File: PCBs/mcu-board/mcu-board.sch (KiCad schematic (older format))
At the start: 7 parts, among them J1 ENCODER-PANEL-1, J2 ENCODER-PANEL-2, J3 5V, J4 3.3V, J5 MDAC-INPUT-SELECTOR, U1 m0-express

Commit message: Updating mcu-board PCB
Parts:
- added C1, C2: C, Capacitor_SMD:C_1206_3216Metric_Pad1.42x1.75mm_HandSolder, symbol Device:C
- added H1, H2, H3, H4: MountingHole_Pad, MountingHole:MountingHole_3.2mm_M3_Pad, symbol Mechanical:MountingHole_Pad
- added IR1: Conn_01x03, Connector_Molex:Molex_KK-254_AE-6410-03A_1x03_P2.54mm_Vertical, symbol Connector_Generic:Conn_01x03
- added LED_3V1, LED_5V1: LED, LED_SMD:LED_1206_3216Metric_Pad1.42x1.75mm_HandSolder, symbol Device:LED
- added RLED1, RLED2: R, Resistor_SMD:R_1206_3216Metric_Pad1.42x1.75mm_HandSolder, symbol Device:R
- added U2, U3: SN74AHCT125DR, Package_SO:SOIC-14_3.9x8.7mm_P1.27mm, symbol SN74AHCT125:SN74AHCT125
- gave numbers to parts that had none: 1
- renumbered J4 to 3.3V1, J3 to 5V1
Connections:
- net labels added: BAT, CS_input_selector, CS_mdac_attenuator, IR_SENSOR, MOSI, SCK, encoder_1_A_3v, encoder_1_A_5v, encoder_1_B_3v, encoder_1_B_5v, encoder_1_neopixel_3v, encoder_1_neopixel_5v, encoder_2_A_3v, encoder_2_A_5v, encoder_2_B_3v, encoder_2_B_5v, encoder_2_neopixel_3v, encoder_2_neopixel_5v
- wire segments 13 -> 96
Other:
- moved on the sheet: 3.3V1, 5V1, J1, J2, J5, U1, VBAT1

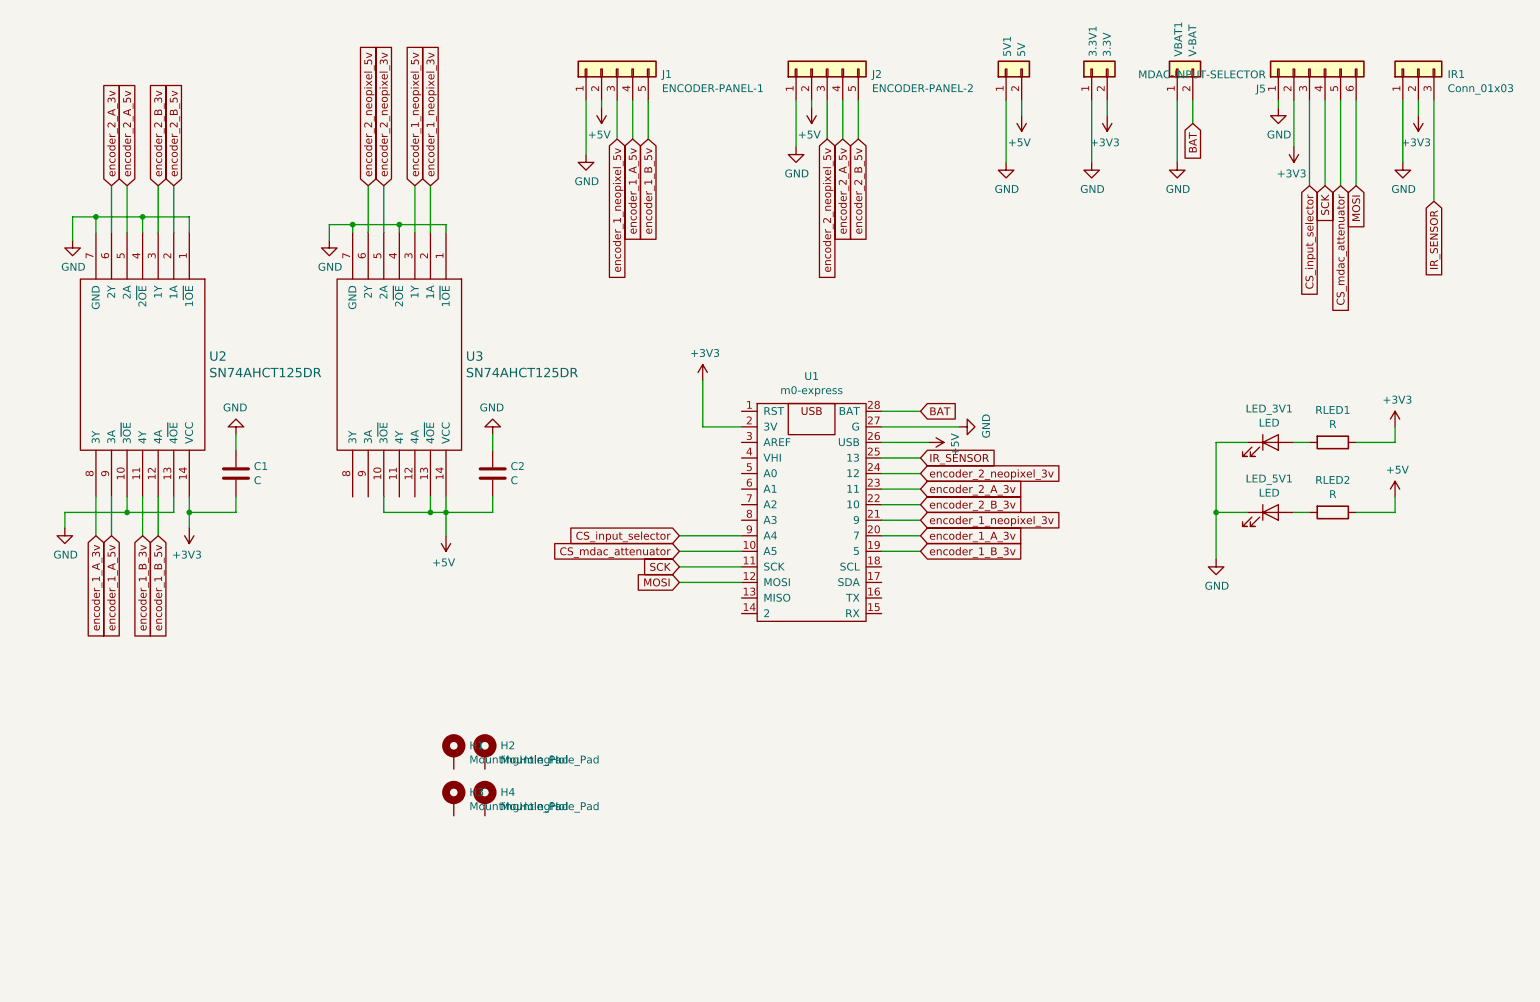
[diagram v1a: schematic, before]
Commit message: renaming some nets
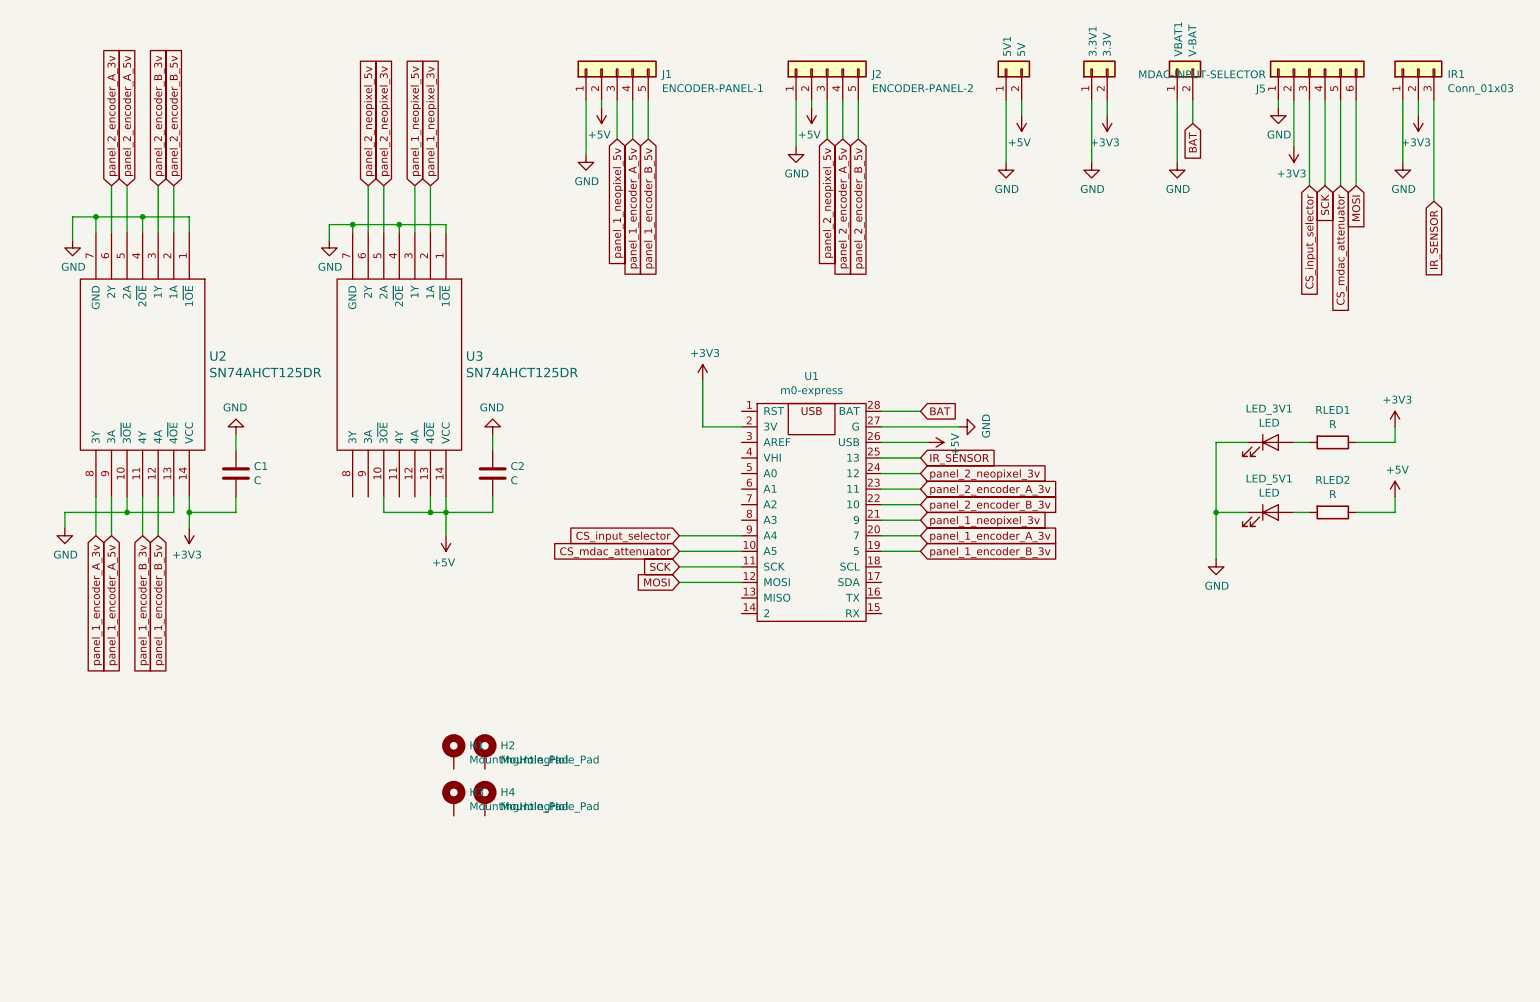
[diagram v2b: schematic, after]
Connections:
- net encoder_1_A_3v renamed panel_1_encoder_A_3v
- net encoder_1_A_5v renamed panel_1_encoder_A_5v
- net encoder_1_B_3v renamed panel_1_encoder_B_3v
- net encoder_1_B_5v renamed panel_1_encoder_B_5v
- net encoder_1_neopixel_3v renamed panel_1_neopixel_3v
- net encoder_1_neopixel_5v renamed panel_1_neopixel_5v
- net encoder_2_A_3v renamed panel_2_encoder_A_3v
- net encoder_2_A_5v renamed panel_2_encoder_A_5v
- net encoder_2_B_3v renamed panel_2_encoder_B_3v
- net encoder_2_B_5v renamed panel_2_encoder_B_5v
- net encoder_2_neopixel_3v renamed panel_2_neopixel_3v
- net encoder_2_neopixel_5v renamed panel_2_neopixel_5v
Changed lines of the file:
@@
 	3350 2650 3350 2350
 Text GLabel 3450 2350 1    50   Input ~ 0
-encoder_1_neopixel_3v
+panel_1_neopixel_3v
 Text GLabel 3150 2350 1    50   Input ~ 0
-encoder_2_neopixel_3v
+panel_2_neopixel_3v
 Text GLabel 6600 4500 2    50   Input ~ 0
-encoder_1_neopixel_3v
+panel_1_neopixel_3v
 Text GLabel 6600 4200 2    50   Input ~ 0
-encoder_2_neopixel_3v
+panel_2_neopixel_3v
 Text GLabel 3050 2350 1    50   Input ~ 0
-encoder_2_neopixel_5v
+panel_2_neopixel_5v
 Text GLabel 3350 2350 1    50   Input ~ 0
-encoder_1_neopixel_5v
+panel_1_neopixel_5v
 Wire Wire Line
 	3550 2650 3550 2600
@@
 Wire Wire Line
 	3150 4450 3450 4450
-Wire Wire Line
-	3550 4450 3550 4600
 Wire Wire Line
 	3550 4350 3550 4450
@@
 $EndComp
 Text GLabel 1500 2350 1    50   Input ~ 0
-encoder_2_A_5v
+panel_2_encoder_A_5v
 Text GLabel 1800 2350 1    50   Input ~ 0
-encoder_2_B_5v
+panel_2_encoder_B_5v
 Wire Wire Line
 	1500 2650 1500 2350
@@
 	1800 2650 1800 2350
 Text GLabel 1400 2350 1    50   Input ~ 0
-encoder_2_A_3v
+panel_2_encoder_A_3v
 Text GLabel 1700 2350 1    50   Input ~ 0
-encoder_2_B_3v
-Wire Wire Line
-	1400 2350 1400 2650
-Wire Wire Line
-	1700 2350 1700 2650
+panel_2_encoder_B_3v
 Text GLabel 6600 4400 2    50   Input ~ 0
-encoder_2_B_3v
+panel_2_encoder_B_3v
 Text GLabel 6600 4300 2    50   Input ~ 0
-encoder_2_A_3v
+panel_2_encoder_A_3v
 Text GLabel 1300 4600 3    50   Input ~ 0
-encoder_1_A_3v
+panel_1_encoder_A_3v
 Text GLabel 1400 4600 3    50   Input ~ 0
-encoder_1_A_5v
+panel_1_encoder_A_5v
 Text GLabel 1600 4600 3    50   Input ~ 0
-encoder_1_B_3v
+panel_1_encoder_B_3v
 Text GLabel 1700 4600 3    50   Input ~ 0
-encoder_1_B_5v
-Wire Wire Line
-	1600 4350 1600 4600
+panel_1_encoder_B_5v
 Wire Wire Line
 	1700 4350 1700 4600
 Wire Wire Line
 	1400 4600 1400 4350
-Wire Wire Line
-	1300 4350 1300 4600
 Text GLabel 6600 4700 2    50   Input ~ 0
-encoder_1_B_3v
+panel_1_encoder_B_3v
 Text GLabel 6600 4600 2    50   Input ~ 0
-encoder_1_A_3v
+panel_1_encoder_A_3v
 $Comp
 L power:+3V3 #PWR0119
@@
 	-1   0    0    1
 $EndComp
-Wire Wire Line
-	1900 4550 1900 4450
 $Comp
 L Device:LED LED_3V1
@@
 	8350 1800 8350 1950
 Wire Wire Line
-	3150 2650 3150 2350
-Wire Wire Line
-	3450 2650 3450 2350
-Wire Wire Line
 	2950 2600 2800 2600
 Wire Wire Line
@@
 Connection ~ 1300 2550
 Wire Wire Line
-	6350 4200 6600 4200
-Wire Wire Line
-	6350 4300 6600 4300
-Wire Wire Line
 	6350 4400 6600 4400
 Wire Wire Line
@@
 	6350 4700 6600 4700
 Text GLabel 6000 2050 3    50   Input ~ 0
-encoder_2_neopixel_5v
+panel_2_neopixel_5v
 Text GLabel 4650 2050 3    50   Input ~ 0
-encoder_1_neopixel_5v
+panel_1_neopixel_5v
 Text GLabel 6200 2050 3    50   Input ~ 0
-encoder_2_B_5v
+panel_2_encoder_B_5v
 Text GLabel 6100 2050 3    50   Input ~ 0
-encoder_2_A_5v
+panel_2_encoder_A_5v
 Text GLabel 4850 2050 3    50   Input ~ 0
-encoder_1_B_5v
+panel_1_encoder_B_5v
 Text GLabel 4750 2050 3    50   Input ~ 0
-encoder_1_A_5v
+panel_1_encoder_A_5v
 Wire Wire Line
 	6000 1800 6000 2050
@@
 Wire Wire Line
 	2200 4450 2200 4350
-Connection ~ 1900 4450
 Wire Wire Line
 	1900 4450 1900 4350
@@
 	-1   0    0    1
 $EndComp
+Wire Wire Line
+	1400 2650 1400 2350
+Wire Wire Line
+	3150 2650 3150 2350
+Wire Wire Line
+	1700 2650 1700 2350
+Wire Wire Line
+	3450 2650 3450 2350
+Wire Wire Line
+	1300 4600 1300 4350
+Wire Wire Line
+	1600 4600 1600 4350
+Wire Wire Line
+	1900 4450 1900 4550
+Connection ~ 1900 4450
+Wire Wire Line
+	3550 4450 3550 4600
+Wire Wire Line
+	6600 4200 6350 4200
+Wire Wire Line
+	6350 4300 6600 4300
 $EndSCHEMATC

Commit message: starting to fix silkscreen
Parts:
- renumbered J1 to ENCODER-PANEL-1, J2 to ENCODER-PANEL-2
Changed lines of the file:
@@
 $EndDescr
 $Comp
-L Connector_Generic:Conn_01x05 J2
+L Connector_Generic:Conn_01x05 ENCODER-PANEL-2
 U 1 1 5C266616
 P 6000 1600
-F 0 "J2" V 5966 1312 50  0000 R CNN
+F 0 "ENCODER-PANEL-2" V 5966 1312 50  0000 R CNN
 F 1 "ENCODER-PANEL-2" V 5875 1312 50  0000 R CNN
 F 2 "Connector_Molex:Molex_KK-254_AE-6410-05A_1x05_P2.54mm_Vertical" H 6000 1600 50  0001 C CNN
@@
 $EndComp
 $Comp
-L Connector_Generic:Conn_01x05 J1
+L Connector_Generic:Conn_01x05 ENCODER-PANEL-1
 U 1 1 5C26667B
 P 4650 1600
-F 0 "J1" V 4616 1312 50  0000 R CNN
+F 0 "ENCODER-PANEL-1" V 4616 1312 50  0000 R CNN
 F 1 "ENCODER-PANEL-1" V 4525 1312 50  0000 R CNN
 F 2 "Connector_Molex:Molex_KK-254_AE-6410-05A_1x05_P2.54mm_Vertical" H 4650 1600 50  0001 C CNN
@@
 Wire Wire Line
 	6350 4300 6600 4300
+$Comp
+L Graphic:Logo_Open_Hardware_Large #LOGO1
+U 1 1 5C596626
+P 1200 7150
+F 0 "#LOGO1" H 1200 7650 50  0001 C CNN
+F 1 "Logo_Open_Hardware_Large" H 1200 6750 50  0001 C CNN
+F 2 "" H 1200 7150 50  0001 C CNN
+F 3 "~" H 1200 7150 50  0001 C CNN
+	1    1200 7150
+	1    0    0    -1
+$EndComp
 $EndSCHEMATC

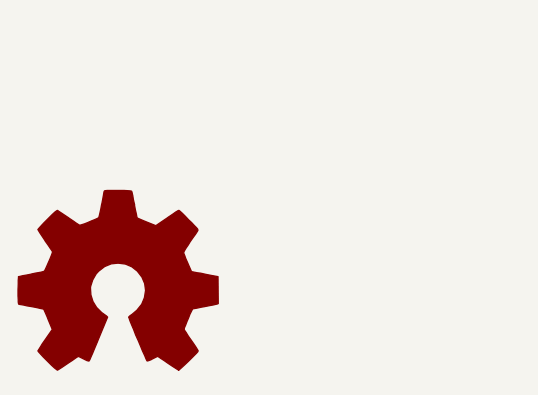
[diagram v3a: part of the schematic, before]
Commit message: change pad/mask clearance
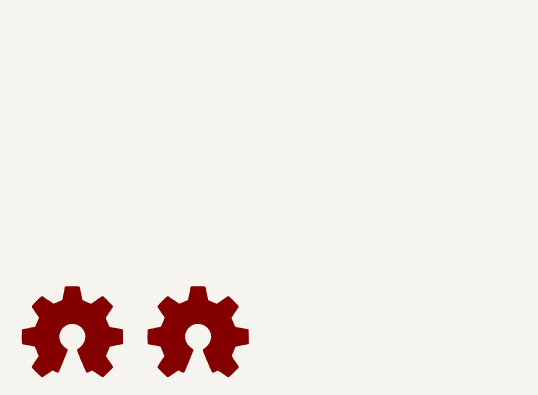
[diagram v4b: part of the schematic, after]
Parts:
- added LOGO1, LOGO2: Logo_Open_Hardware_Small, Symbol:OSHW-Logo2_14.6x12mm_SilkScreen, symbol Graphic:Logo_Open_Hardware_Small
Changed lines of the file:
@@
 	6350 4300 6600 4300
 $Comp
-L Graphic:Logo_Open_Hardware_Large #LOGO1
-U 1 1 5C596626
-P 1200 7150
-F 0 "#LOGO1" H 1200 7650 50  0001 C CNN
-F 1 "Logo_Open_Hardware_Large" H 1200 6750 50  0001 C CNN
-F 2 "" H 1200 7150 50  0001 C CNN
-F 3 "~" H 1200 7150 50  0001 C CNN
-	1    1200 7150
+L Graphic:Logo_Open_Hardware_Small LOGO1
+U 1 1 5C4FB3BF
+P 1000 7350
+F 0 "LOGO1" H 1000 7625 50  0001 C CNN
+F 1 "Logo_Open_Hardware_Small" H 1000 7125 50  0001 C CNN
+F 2 "Symbol:OSHW-Logo2_14.6x12mm_SilkScreen" H 1000 7350 50  0001 C CNN
+F 3 "~" H 1000 7350 50  0001 C CNN
+	1    1000 7350
 	1    0    0    -1
 $EndComp
+$Comp
+L Graphic:Logo_Open_Hardware_Small LOGO2
+U 1 1 5C4FB40D
+P 1550 7350
+F 0 "LOGO2" H 1550 7625 50  0001 C CNN
+F 1 "Logo_Open_Hardware_Small" H 1550 7125 50  0001 C CNN
+F 2 "Symbol:OSHW-Logo2_14.6x12mm_SilkScreen" H 1550 7350 50  0001 C CNN
+F 3 "~" H 1550 7350 50  0001 C CNN
+	1    1550 7350
+	1    0    0    -1
+$EndComp

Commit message: misc updates
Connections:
- net panel_2_encoder_A_3v: now also U1.22 (10), U2.3 (1Y); no longer U1.23 (11), U2.6 (2Y)
- net panel_2_encoder_A_5v: now also ENCODER-PANEL-2.5 (Pin_5), U2.2 (1A); no longer ENCODER-PANEL-2.4 (Pin_4), U2.5 (2A)
- net panel_2_encoder_B_3v: now also U1.23 (11), U2.6 (2Y); no longer U1.22 (10), U2.3 (1Y)
- net panel_2_encoder_B_5v: now also ENCODER-PANEL-2.4 (Pin_4), U2.5 (2A); no longer ENCODER-PANEL-2.5 (Pin_5), U2.2 (1A)
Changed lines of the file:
@@
 $EndComp
 Text GLabel 1500 2350 1    50   Input ~ 0
+panel_2_encoder_B_5v
+Text GLabel 1800 2350 1    50   Input ~ 0
 panel_2_encoder_A_5v
-Text GLabel 1800 2350 1    50   Input ~ 0
-panel_2_encoder_B_5v
 Wire Wire Line
 	1500 2650 1500 2350
@@
 	1800 2650 1800 2350
 Text GLabel 1400 2350 1    50   Input ~ 0
+panel_2_encoder_B_3v
+Text GLabel 1700 2350 1    50   Input ~ 0
 panel_2_encoder_A_3v
-Text GLabel 1700 2350 1    50   Input ~ 0
+Text GLabel 6600 4400 2    50   Input ~ 0
+panel_2_encoder_A_3v
+Text GLabel 6600 4300 2    50   Input ~ 0
 panel_2_encoder_B_3v
-Text GLabel 6600 4400 2    50   Input ~ 0
-panel_2_encoder_B_3v
-Text GLabel 6600 4300 2    50   Input ~ 0
-panel_2_encoder_A_3v
 Text GLabel 1300 4600 3    50   Input ~ 0
 panel_1_encoder_A_3v
@@
 panel_1_neopixel_5v
 Text GLabel 6200 2050 3    50   Input ~ 0
+panel_2_encoder_A_5v
+Text GLabel 6100 2050 3    50   Input ~ 0
 panel_2_encoder_B_5v
-Text GLabel 6100 2050 3    50   Input ~ 0
-panel_2_encoder_A_5v
 Text GLabel 4850 2050 3    50   Input ~ 0
 panel_1_encoder_B_5v
